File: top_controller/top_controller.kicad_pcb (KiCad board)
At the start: 2 copper layers, 117 parts, among them J1 OUT1, J10 USB_C_Receptacle_USB2.0, J11 SWD, J12 UART, J13 BOOT0, J14 BOOT1, J2 OUT2, J3 OUT3, J4 OUT4, J5 OUT5, J6 OUT6, J7 OUT7, J8 OUT8, J9 PIN, SW1 RESET, U1 STM32F103C8Tx, U2 LT3045xMSE, U3 AD5754BREZ, U4 AD5754BREZ, U5 REF192, U6 EPM78V2, U7 REF192, Y1 8MHz

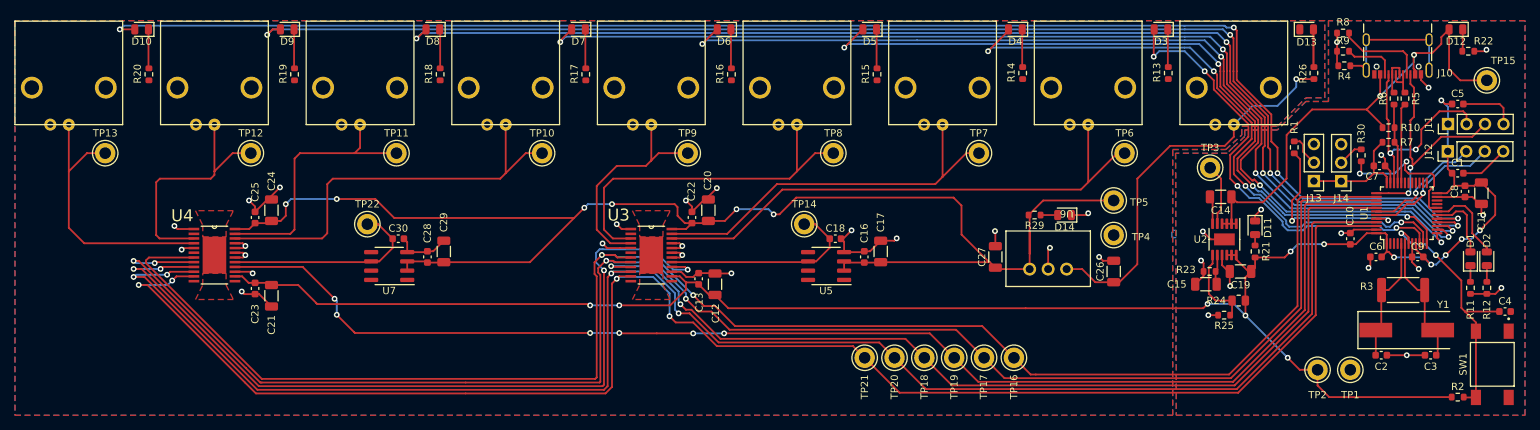
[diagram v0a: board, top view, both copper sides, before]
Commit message: Fixed a bunch of DRC errors - Fixed couple place where 3v3 was not routed - Allowed for 1 connection between pad and thermal relief (cause kicad counts just connectin a pad to the ground plane as thermal relief) - Deleted some tiny phantom tracks
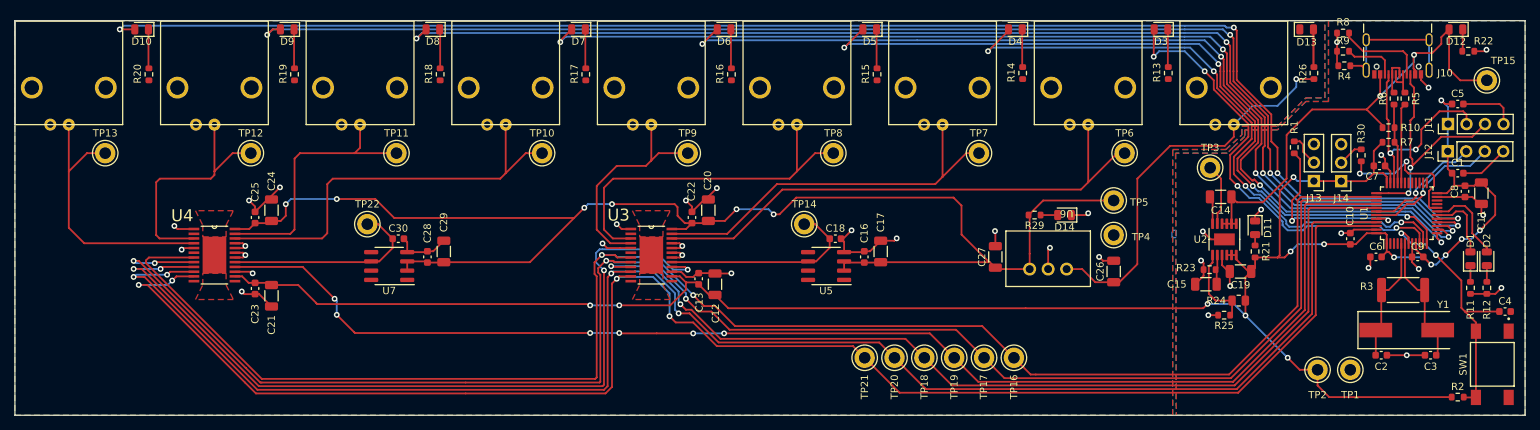
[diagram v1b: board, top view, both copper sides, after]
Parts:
- moved R23 0.25 mm to (196.7, 65.0)
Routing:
- net +3V3: track 282.0 -> 296.9 mm, vias 13 -> 14
- net VDDA: track 198.0 -> 195.0 mm
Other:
- board outline added: 207.4 x 54.2 mm
